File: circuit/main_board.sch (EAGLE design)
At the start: 9 parts

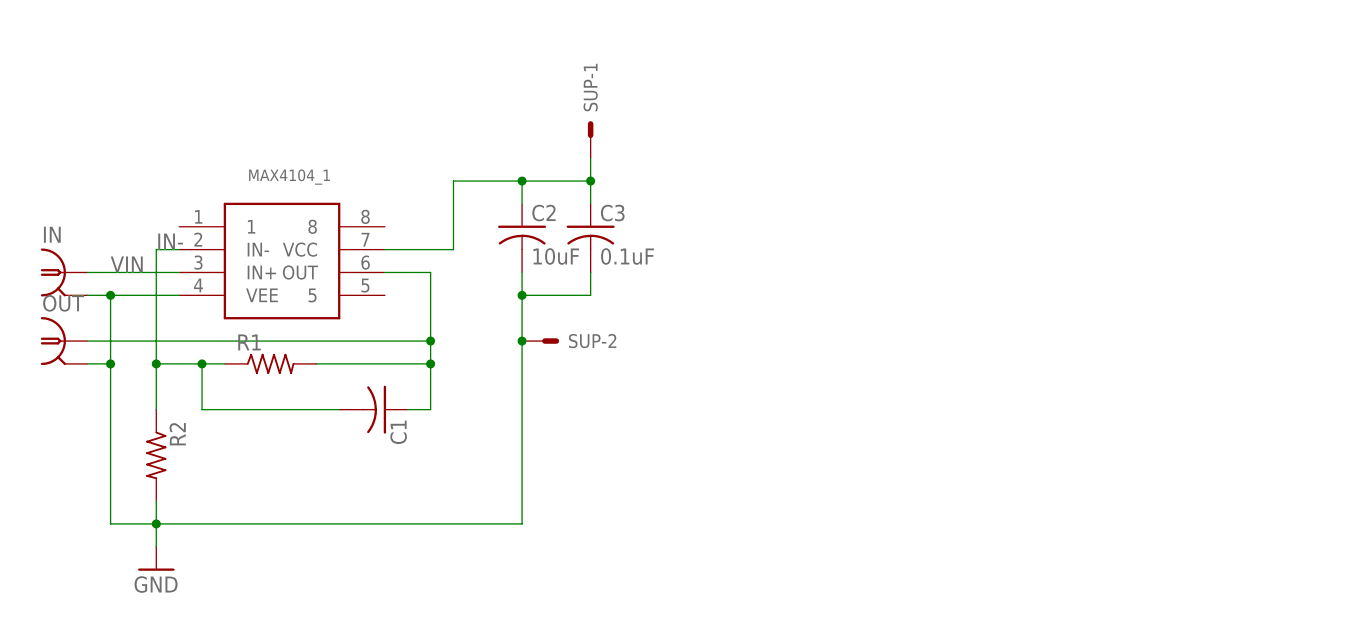
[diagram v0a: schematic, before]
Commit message: Added Schottky diode to Library; added Peak Detector to Schematic and Board
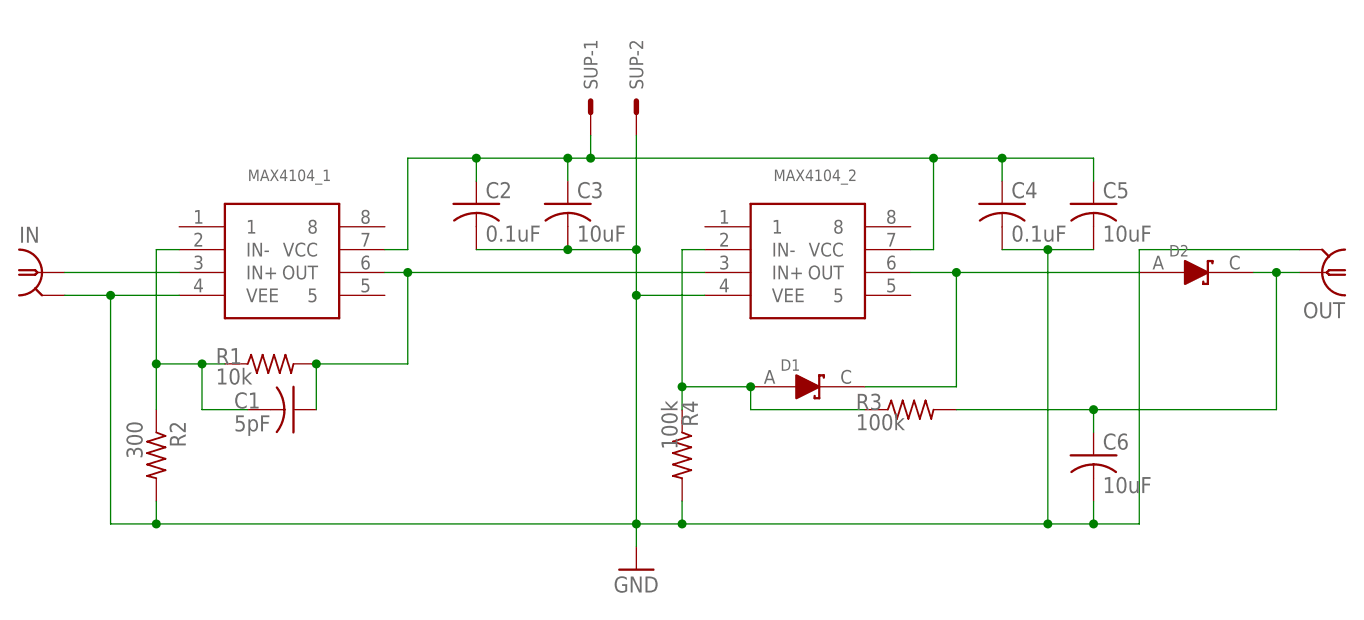
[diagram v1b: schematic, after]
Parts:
- added C4: 0.1uF, rcl:C-USC0805
- added C5, C6: 10uF, rcl:C-USC0805
- added D1, D2: (no value), 000phys605parts:SCH_D1
- added MAX4104_2: (no value), 000phys605parts:MAX4104
- added R3, R4: 100k, rcl:R-US_M0805
- C1: value (none) -> 5pF
- C2: value 10uF -> 0.1uF
- C3: value 0.1uF -> 10uF
- R1: value (none) -> 10k
- R2: value (none) -> 300
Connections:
- net IN- renamed IN-_1
- net VIN renamed IN
- removed net N$2: C2.1, C3.1, MAX4104_1.VCC, SUP-1.S
- removed net VOUT: C1.1, MAX4104_1.OUT, OUT.1, R1.2
- new net AMP: C1.1, MAX4104_1.OUT, MAX4104_2.IN+, R1.2
- new net DIG_READOUT: C6.1, D2.OUT, OUT.1, R3.2
- new net IN-_2: D1.IN, MAX4104_2.IN-, R3.1, R4.1
- new net OUT_2: D1.OUT, D2.IN, MAX4104_2.OUT
- new net VCC: C2.1, C3.1, C4.1, C5.1, MAX4104_1.VCC, MAX4104_2.VCC, SUP-1.S
- net GND: now also C4.2, C5.2, C6.2, MAX4104_2.VEE, R4.2
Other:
- moved on the sheet: C1, C2, C3, IN, OUT, SUP-1, SUP-2
